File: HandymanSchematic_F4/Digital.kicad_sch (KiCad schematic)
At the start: 31 parts, among them J1 SWD Header, J2 PWR, J3 JACKS, J4 FOOTSWITCH, J5 ScopeGroundLoop, Q2 2N7002, Q3 2N7002, SW1 RST, SW2 BYP, U3 STM32G030F6P6, U4 AMS1117, U5 SSD1306

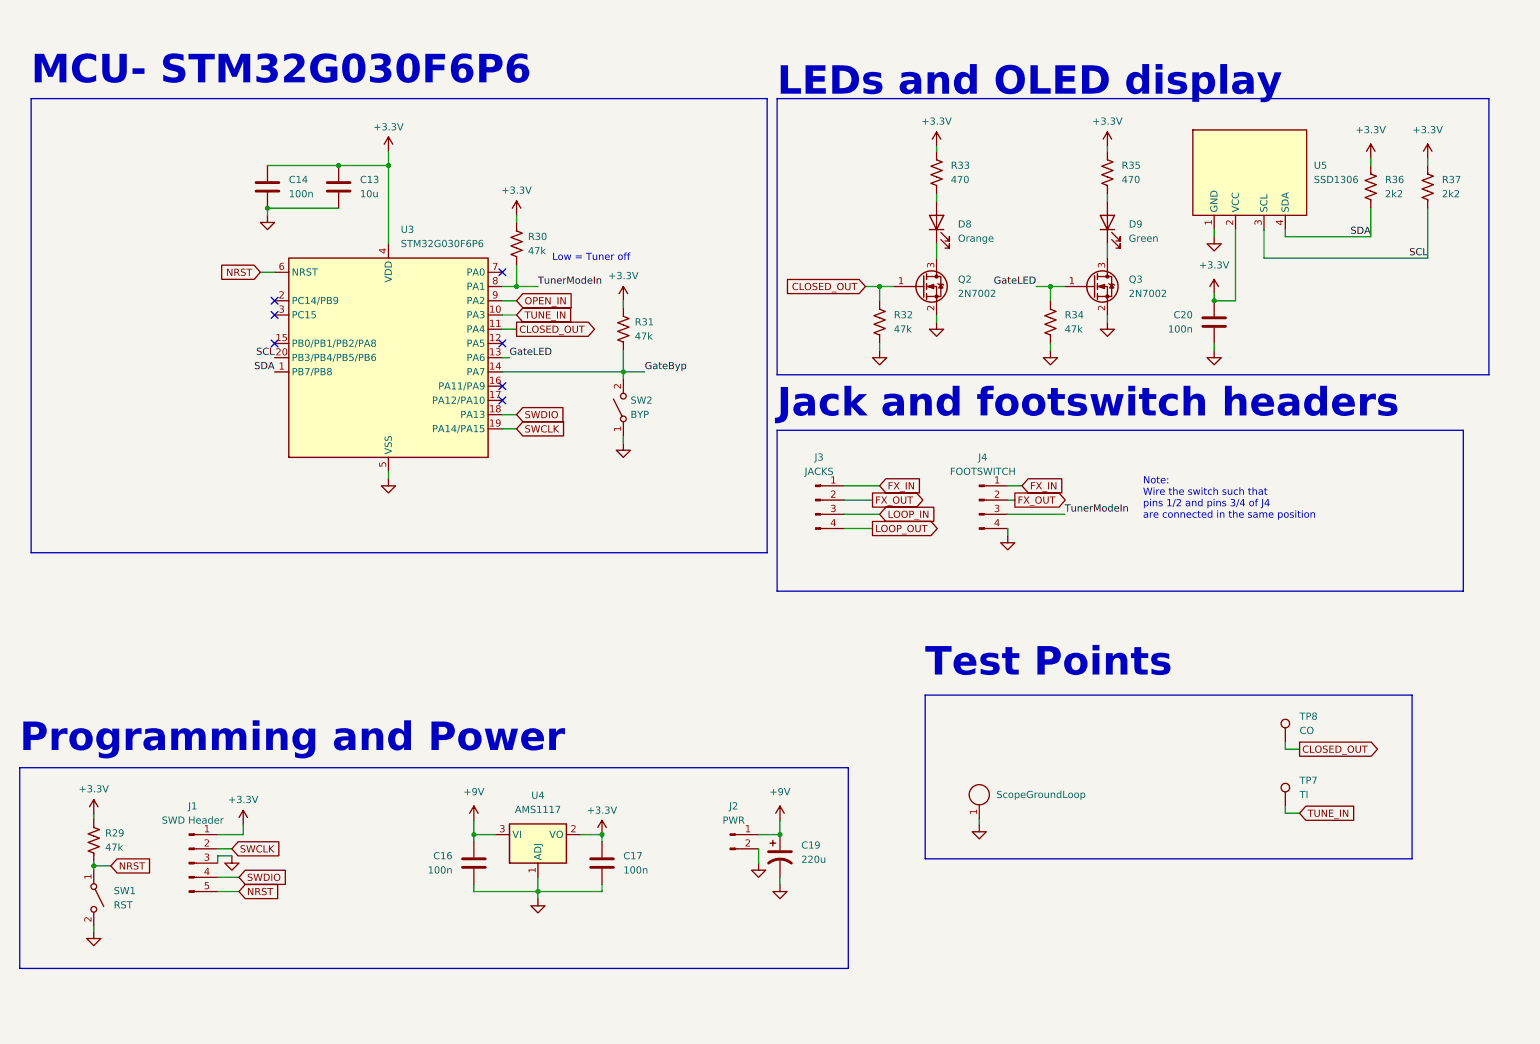
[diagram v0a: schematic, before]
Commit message: F4 wired up on schem, footprints assigned
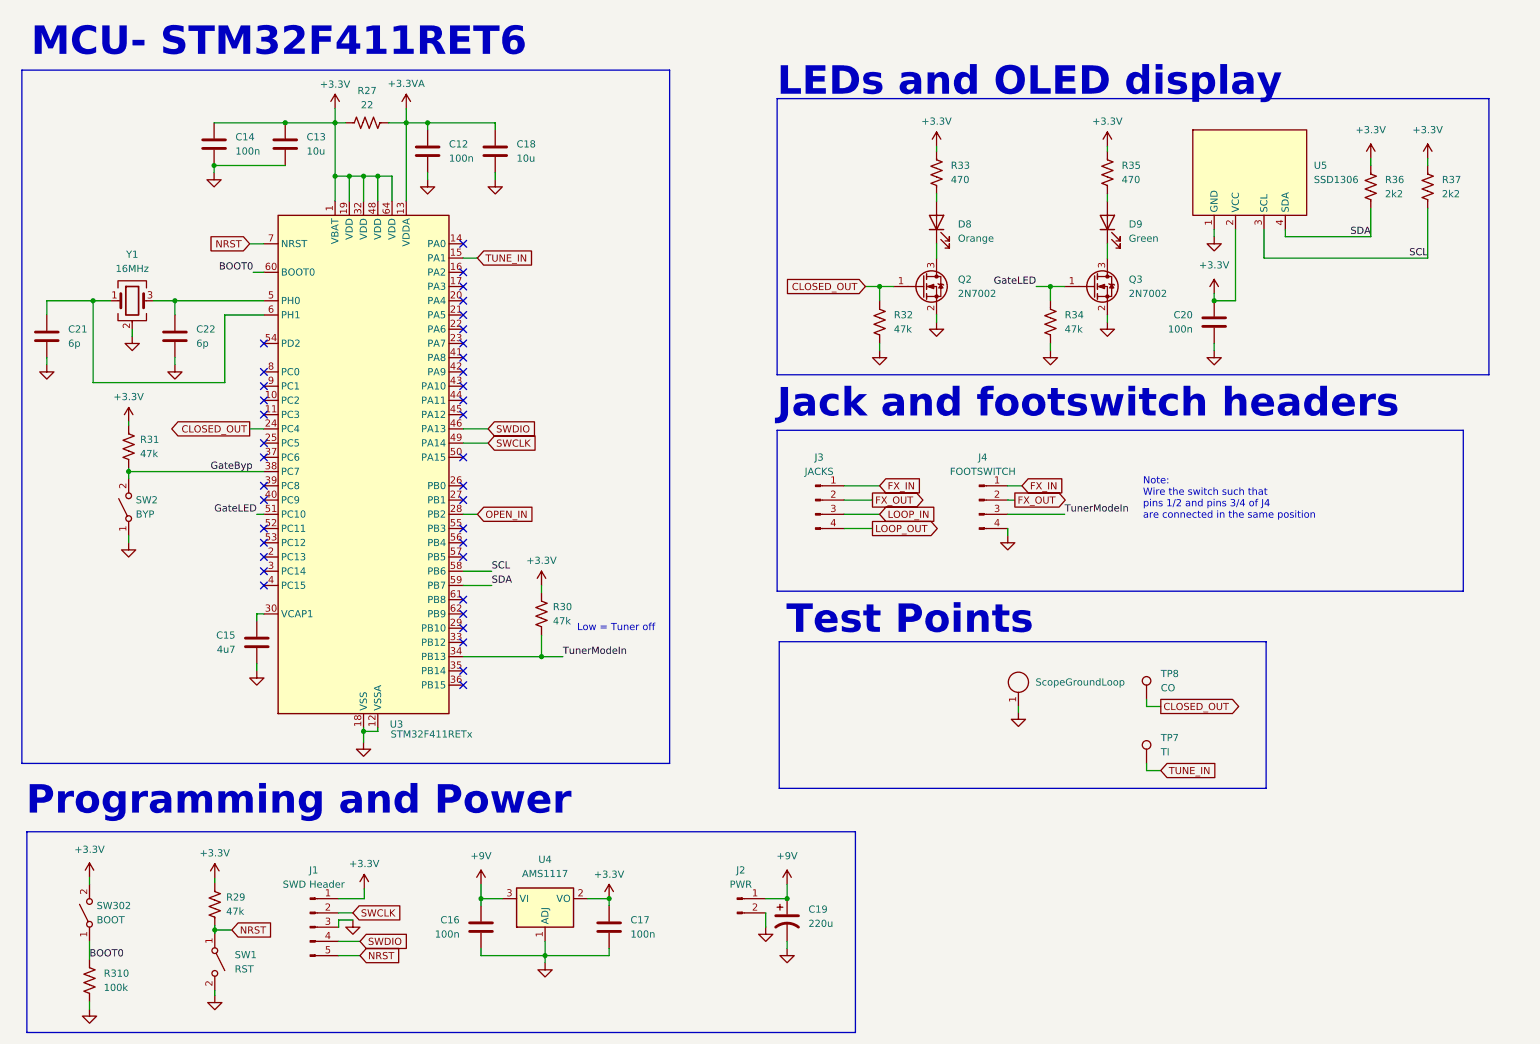
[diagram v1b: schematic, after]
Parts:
- removed U3: STM32G030F6P6, Package_SO:TSSOP-20_4.4x6.5mm_P0.65mm, symbol MCU_ST_STM32G0:STM32G030F6Px
- added C12: 100n, Capacitor_SMD:C_0805_2012Metric, symbol Device:C
- added C15: 4u7, Capacitor_SMD:C_0805_2012Metric, symbol Device:C
- added C18: 10u, Capacitor_SMD:C_0805_2012Metric, symbol Device:C
- added C21, C22: 6p, Capacitor_SMD:C_0805_2012Metric, symbol Device:C
- added R27: 22, Resistor_SMD:R_0805_2012Metric, symbol Device:R_US
- added R310: 100k, Resistor_SMD:R_0805_2012Metric, symbol Device:R_US
- added SW302: BOOT, Button_Switch_SMD:SW_SPST_B3U-1000P, symbol Switch:SW_SPST
- added U3: STM32F411RETx, Package_QFP:LQFP-64_10x10mm_P0.5mm, symbol MCU_ST_STM32F4:STM32F411RETx
- added Y1: 16MHz, Crystal:Crystal_SMD_3225-4Pin_3.2x2.5mm, symbol Device:Crystal_GND24
- J5: footprint Connector:THT_GND_WIRE -> Connector_Wire:THT_GND_WIRE
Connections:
- net +3.3V: now also R27.1, SW302.2 (B), U3.1 (VBAT), U3.19 (VDD), U3.32 (VDD), U3.48 (VDD), U3.64 (VDD)
- net CLOSED_OUT: now also U3.24 (PC4)
- net GND: now also C12.1, C15.1, C18.1, C21.1, C22.1, R310.2, U3.12 (VSSA), U3.18 (VSS), U3.31 (VSS), U3.47 (VSS), U3.63 (VSS), Y1.2 (G), Y1.4 (G)
- net GateByp: now also U3.38 (PC7)
- net GateLED: now also U3.51 (PC10)
- net NRST: now also U3.7 (NRST)
- net OPEN_IN: now also U3.28 (PB2)
- net SCL: now also U3.58 (PB6)
- net SDA: now also U3.59 (PB7)
- net SWCLK: now also U3.49 (PA14)
- net SWDIO: now also U3.46 (PA13)
- net TUNE_IN: now also U3.15 (PA1)
- net TunerModeIn: now also U3.34 (PB13)
- new net: C15.2, U3.30 (VCAP1)
- new net: C22.2, U3.5 (PH0), Y1.3
- new net: C21.2, U3.6 (PH1), Y1.1
- new net +3.3VA: C12.2, C18.2, R27.2, U3.13 (VDDA)
- new net BOOT0: R310.1, SW302.1 (A), U3.60 (BOOT0)
- no-connect marks 7 -> 38
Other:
- note added: "MCU- STM32F411RET6"
- note removed: "MCU- STM32G030F6P6"
- moved on the sheet: C13, C14, C16, C17, C19, J1, J2, R29, R30, R31, SW1, SW2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

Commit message: switched to firmware env, new layout
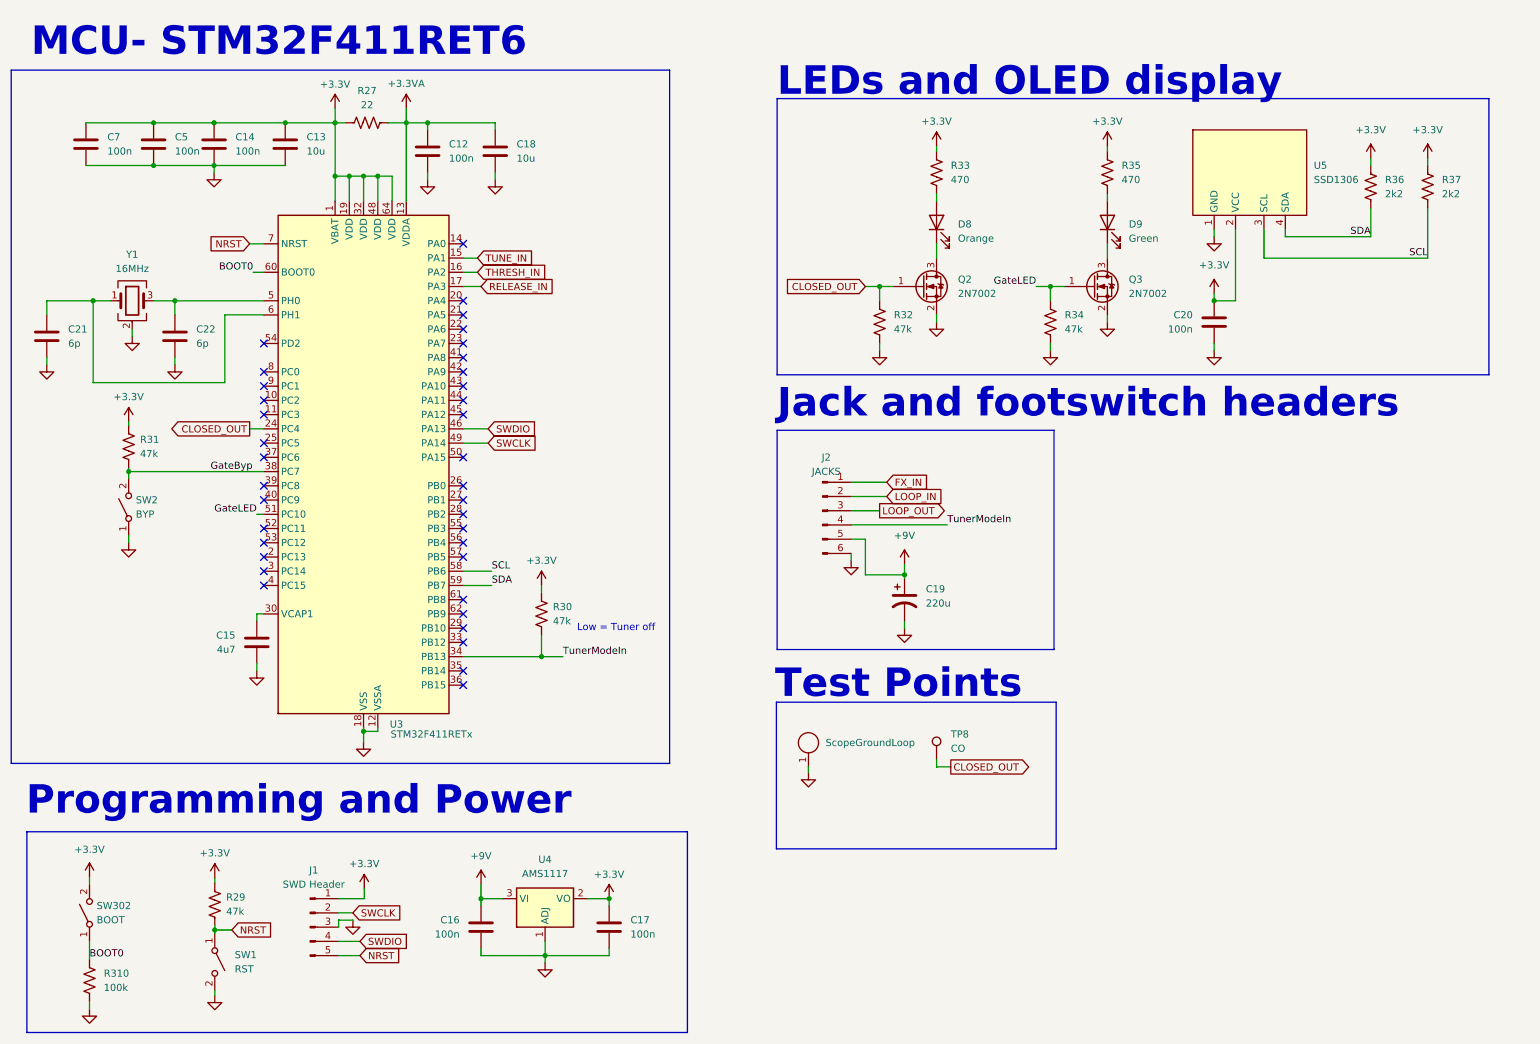
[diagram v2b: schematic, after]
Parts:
- removed J2: PWR, Connector_PinHeader_2.54mm:PinHeader_1x02_P2.54mm_Vertical, symbol Connector:Conn_01x02_Pin
- removed J3: JACKS, Connector_PinHeader_2.54mm:PinHeader_1x04_P2.54mm_Vertical, symbol Connector:Conn_01x04_Pin
- removed J4: FOOTSWITCH, Connector_PinHeader_2.54mm:PinHeader_1x04_P2.54mm_Vertical, symbol Connector:Conn_01x04_Pin
- removed TP7: TI, TestPoint:TestPoint_THTPad_D2.0mm_Drill1.0mm_VAL, symbol Connector:TestPoint
- added C5, C7: 100n, Capacitor_SMD:C_0805_2012Metric, symbol Device:C
- added J2: JACKS, Connector_PinHeader_2.00mm:PinHeader_1x06_P2.00mm_Vertical, symbol Connector:Conn_01x06_Pin
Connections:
- net +3.3V: now also C5.2, C7.2
- net +9V: now also J2.5 (Pin_5)
- net FX_IN: now also J2.1 (Pin_1)
- net GND: now also C5.1, C7.1, J2.6 (Pin_6)
- net LOOP_IN: now also J2.2 (Pin_2)
- net LOOP_OUT: now also J2.3 (Pin_3)
- net TunerModeIn: now also J2.4 (Pin_4)
- net THRESH_IN: now reaches U3.16 (PA2)
- net RELEASE_IN: now reaches U3.17 (PA3)
- net OPEN_IN: no longer names the net of U3.28 (PB2)
- no-connect marks 38 -> 37
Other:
- note removed: "Note: Wire the switch such that pins 1/2 and pins 3/4 of J4 are connected in the same position"
- moved on the sheet: C19, TP8

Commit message: v2 gerbers ready
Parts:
- added TP3: TI, TestPoint:TestPoint_THTPad_D2.0mm_Drill1.0mm_VAL, symbol Connector:TestPoint
- J2: footprint Connector_PinHeader_2.00mm:PinHeader_1x06_P2.00mm_Vertical -> Connector_PinHeader_2.54mm:PinHeader_1x06_P2.54mm_Vertical
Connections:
- net TUNE_IN: now also TP3.1
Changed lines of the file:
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@@
+	(wire
+		(pts
+			(xy 180.34 155.575) (xy 177.8 155.575)
+		)
+		(stroke
+			(width 0)
+			(type default)
+		)
+	)
 	(wire
 		(pts
@@
 		(pts
 			(xy 50.8 66.04) (xy 57.785 66.04)
+		)
+		(stroke
+			(width 0)
+			(type default)
+		)
+	)
+	(wire
+		(pts
+			(xy 177.8 155.575) (xy 177.8 154.305)
 		)
 		(stroke
@@
 		(property "Intersheetrefs" "${INTERSHEET_REFS}"
 			(at 180.1805 100.965 0)
+			(effects
+				(font
+					(size 1.27 1.27)
+				)
+				(justify left)
+				(hide yes)
+			)
+		)
+	)
+	(global_label "TUNE_IN"
+		(shape output)
+		(at 180.34 155.575 0)
+		(fields_autoplaced yes)
+		(effects
+			(font
+				(size 1.27 1.27)
+			)
+			(justify left)
+		)
+		(property "Intersheetrefs" "${INTERSHEET_REFS}"
+			(at 191.0057 155.575 0)
 			(effects
 				(font
@@
 	)
 	(symbol
+		(lib_id "Connector:TestPoint")
+		(at 177.8 154.305 0)
+		(unit 1)
+		(exclude_from_sim no)
+		(in_bom no)
+		(on_board yes)
+		(dnp no)
+		(fields_autoplaced yes)
+		(property "Reference" "TP3"
+			(at 180.34 149.7329 0)
+			(effects
+				(font
+					(size 1.27 1.27)
+				)
+				(justify left)
+			)
+		)
+		(property "Value" "TI"
+			(at 180.34 152.2729 0)
+			(effects
+				(font
+					(size 1.27 1.27)
+				)
+				(justify left)
+			)
+		)
+		(property "Footprint" "TestPoint:TestPoint_THTPad_D2.0mm_Drill1.0mm_VAL"
+			(at 182.88 154.305 0)
+			(effects
+				(font
+					(size 1.27 1.27)
+				)
+				(hide yes)
+			)
+		)
+		(property "Datasheet" "~"
+			(at 182.88 154.305 0)
+			(effects
+				(font
+					(size 1.27 1.27)
+				)
+				(hide yes)
+			)
+		)
+		(property "Description" "test point"
+			(at 177.8 154.305 0)
+			(effects
+				(font
+					(size 1.27 1.27)
+				)
+				(hide yes)
+			)
+		)
+		(pin "1"
+		)
+		(instances
+			(project "HandymanSchematic_F4"
+				(path "/bc3da82e-d0a7-49a6-b9ec-ecd2040670ff/887caaef-7a77-44c5-aff2-1e54e61c47e4"
+					(reference "TP3")
+					(unit 1)
+				)
+			)
+		)
+	)
+	(symbol
 		(lib_id "power:GND")
 		(at 107.95 181.61 0)
@@
 			)
 		)
-		(property "Footprint" "Connector_PinHeader_2.00mm:PinHeader_1x06_P2.00mm_Vertical"
+		(property "Footprint" "Connector_PinHeader_2.54mm:PinHeader_1x06_P2.54mm_Vertical"
 			(at 157.48 100.965 0)
 			(effects

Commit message: new prelim routing, DRC passing
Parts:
- removed SW302: BOOT, Button_Switch_SMD:SW_SPST_B3U-1000P, symbol Switch:SW_SPST
- R310: value 100k -> 10k
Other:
- moved on the sheet: R310
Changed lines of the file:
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@@
 	(wire
 		(pts
-			(xy 26.67 188.595) (xy 26.67 189.865)
+			(xy 26.035 180.34) (xy 26.035 181.61)
 		)
 		(stroke
@@
 	(wire
 		(pts
-			(xy 26.67 166.37) (xy 26.67 167.64)
-		)
-		(stroke
-			(width 0)
-			(type default)
-		)
-	)
-	(wire
-		(pts
 			(xy 71.12 170.18) (xy 75.692 170.18)
 		)
@@
 	(wire
 		(pts
-			(xy 26.67 177.8) (xy 26.67 180.975)
+			(xy 26.035 169.545) (xy 26.035 172.72)
 		)
 		(stroke
@@
 	)
 	(label "BOOT0"
-		(at 26.67 180.975 0)
+		(at 26.035 169.545 0)
 		(effects
 			(font
@@
 	(symbol
 		(lib_id "Device:R_US")
-		(at 26.67 184.785 0)
+		(at 26.035 176.53 0)
 		(unit 1)
 		(exclude_from_sim no)
@@
 		(fields_autoplaced yes)
 		(property "Reference" "R310"
-			(at 29.21 183.515 0)
+			(at 27.94 175.2599 0)
 			(effects
 				(font
@@
 			)
 		)
-		(property "Value" "100k"
-			(at 29.21 186.055 0)
+		(property "Value" "10k"
+			(at 27.94 177.7999 0)
 			(effects
 				(font
@@
 		)
 		(property "Footprint" "Resistor_SMD:R_0805_2012Metric"
-			(at 27.686 185.039 90)
+			(at 27.051 176.784 90)
 			(effects
 				(font
@@
 		)
 		(property "Datasheet" "~"
-			(at 26.67 184.785 0)
+			(at 26.035 176.53 0)
 			(effects
 				(font
@@
 		)
 		(property "Description" ""
-			(at 26.67 184.785 0)
+			(at 26.035 176.53 0)
 			(effects
 				(font
@@
 	(symbol
 		(lib_id "power:GND")
-		(at 26.67 189.865 0)
+		(at 26.035 181.61 0)
 		(mirror y)
 		(unit 1)
@@
 		(fields_autoplaced yes)
 		(property "Reference" "#PWR0337"
-			(at 26.67 196.215 0)
+			(at 26.035 187.96 0)
 			(effects
 				(font
@@
 		)
 		(property "Value" "GND"
-			(at 26.67 193.675 0)
+			(at 26.035 185.42 0)
 			(effects
 				(font
@@
 		)
 		(property "Footprint" ""
-			(at 26.67 189.865 0)
+			(at 26.035 181.61 0)
 			(effects
 				(font
@@
 		)
 		(property "Datasheet" ""
-			(at 26.67 189.865 0)
+			(at 26.035 181.61 0)
 			(effects
 				(font
@@
 		)
 		(property "Description" ""
-			(at 26.67 189.865 0)
+			(at 26.035 181.61 0)
 			(effects
 				(font
@@
 	)
 	(symbol
-		(lib_id "power:+3.3V")
-		(at 26.67 166.37 0)
-		(unit 1)
-		(exclude_from_sim no)
-		(in_bom yes)
-		(on_board yes)
-		(dnp no)
-		(fields_autoplaced yes)
-		(property "Reference" "#PWR0336"
-			(at 26.67 170.18 0)
-			(effects
-				(font
-					(size 1.27 1.27)
-				)
-				(hide yes)
-			)
-		)
-		(property "Value" "+3.3V"
-			(at 26.67 161.417 0)
-			(effects
-				(font
-					(size 1.27 1.27)
-				)
-			)
-		)
-		(property "Footprint" ""
-			(at 26.67 166.37 0)
-			(effects
-				(font
-					(size 1.27 1.27)
-				)
-				(hide yes)
-			)
-		)
-		(property "Datasheet" ""
-			(at 26.67 166.37 0)
-			(effects
-				(font
-					(size 1.27 1.27)
-				)
-				(hide yes)
-			)
-		)
-		(property "Description" ""
-			(at 26.67 166.37 0)
-			(effects
-				(font
-					(size 1.27 1.27)
-				)
-				(hide yes)
-			)
-		)
-		(pin "1"
-		)
-		(instances
-			(project "HandymanSchematic_F4"
-				(path "/bc3da82e-d0a7-49a6-b9ec-ecd2040670ff/887caaef-7a77-44c5-aff2-1e54e61c47e4"
-					(reference "#PWR0336")
-					(unit 1)
-				)
-			)
-		)
-	)
-	(symbol
 		(lib_id "Device:R_US")
 		(at 33.655 89.535 0)
@@
 					(unit 1)
 				)
-			)
-		)
-	)
-	(symbol
-		(lib_id "Switch:SW_SPST")
-		(at 26.67 172.72 90)
-		(unit 1)
-		(exclude_from_sim no)
-		(in_bom yes)
-		(on_board yes)
-		(dnp no)
-		(fields_autoplaced yes)
-		(property "Reference" "SW302"
-			(at 27.94 171.45 90)
-			(effects
-				(font
-					(size 1.27 1.27)
-				)
-				(justify right)
-			)
-		)
-		(property "Value" "BOOT"
-			(at 27.94 173.99 90)
-			(effects
-				(font
-					(size 1.27 1.27)
-				)
-				(justify right)
-			)
-		)
-		(property "Footprint" "Button_Switch_SMD:SW_SPST_B3U-1000P"
-			(at 26.67 172.72 0)
-			(effects
-				(font
-					(size 1.27 1.27)
-				)
-				(hide yes)
-			)
-		)
-		(property "Datasheet" "~"
-			(at 26.67 172.72 0)
-			(effects
-				(font
-					(size 1.27 1.27)
-				)
-				(hide yes)
-			)
-		)
-		(property "Description" ""
-			(at 26.67 172.72 0)
-			(effects
-				(font
-					(size 1.27 1.27)
-				)
-				(hide yes)
-			)
-		)
-		(pin "1"
-		)
-		(pin "2"
-		)
-		(instances
-			(project "HandymanSchematic_F4"
-				(path "/bc3da82e-d0a7-49a6-b9ec-ecd2040670ff/887caaef-7a77-44c5-aff2-1e54e61c47e4"
-					(reference "SW302")
-					(unit 1)
-				)
